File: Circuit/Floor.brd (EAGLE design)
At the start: 52.5 x 84.9 mm, 27 parts, among them U1 AMS1117-3.3, X2 ESP-12

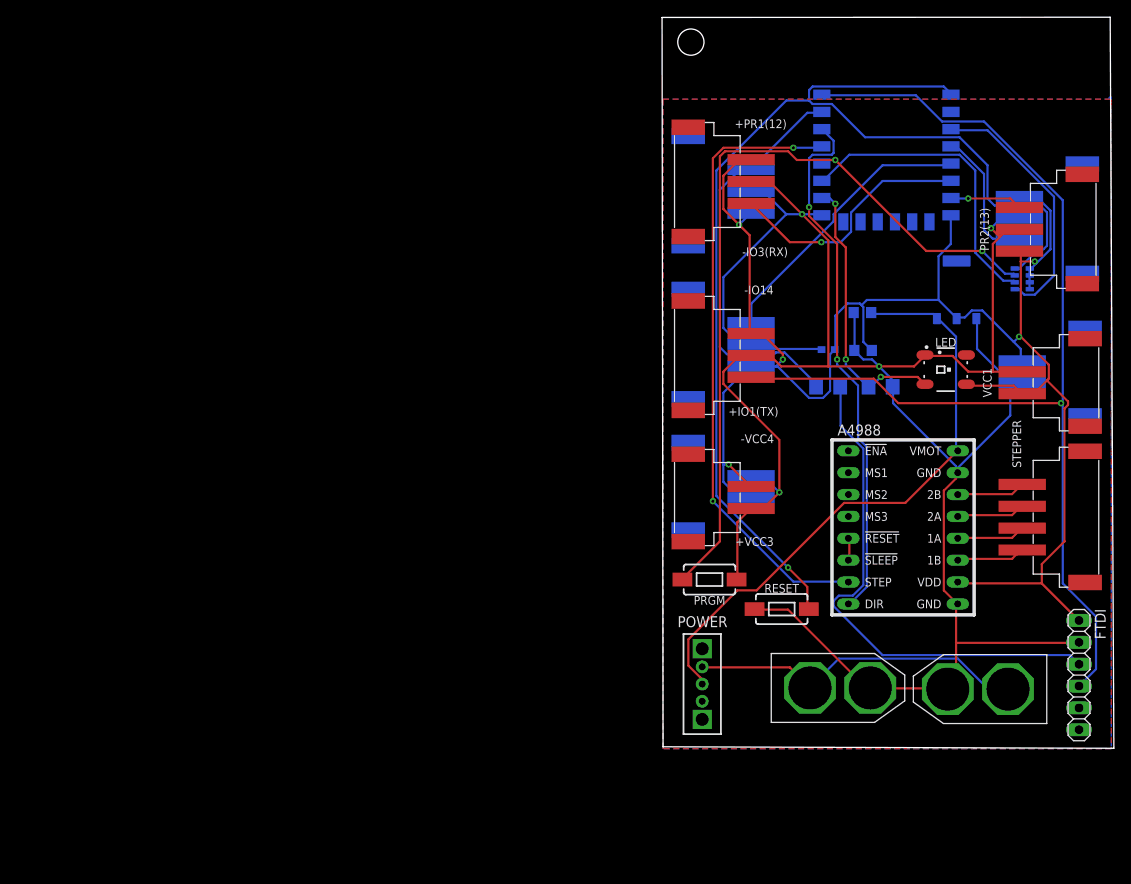
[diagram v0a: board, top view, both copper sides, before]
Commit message: correct flipped xh conns
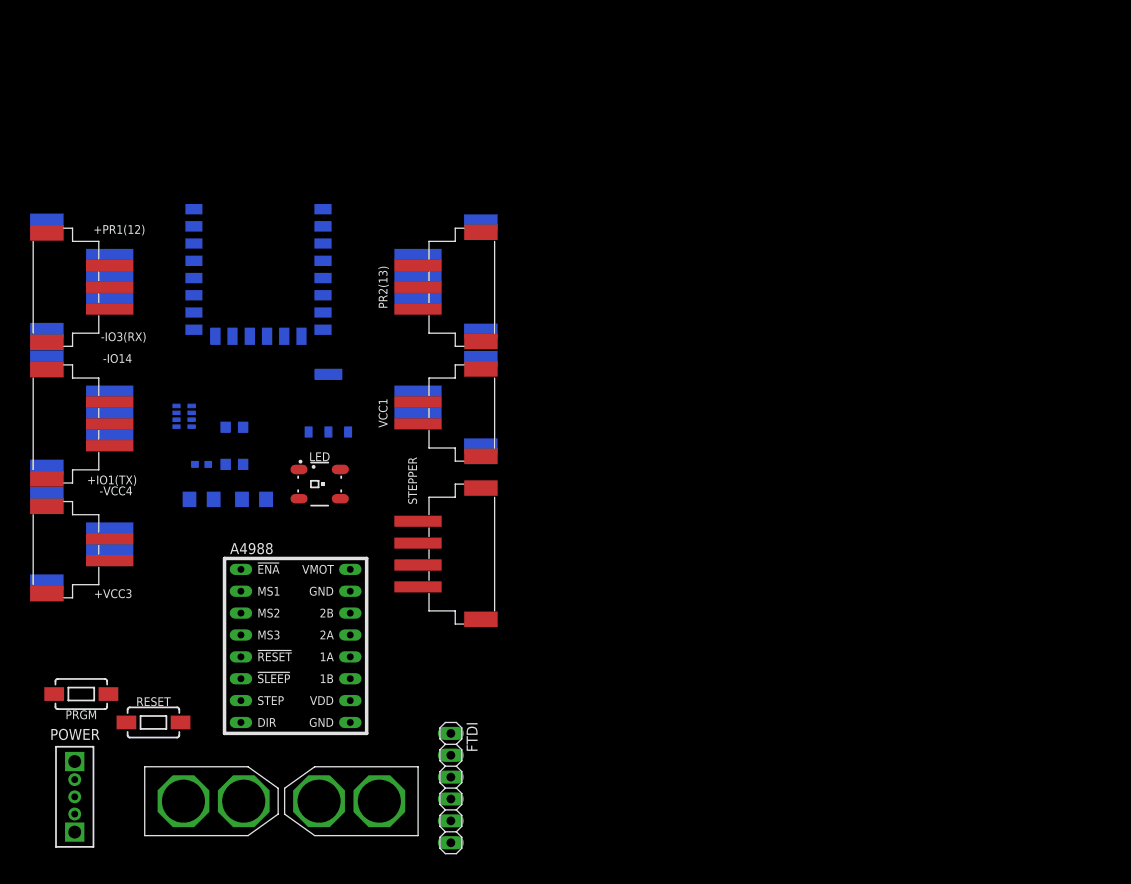
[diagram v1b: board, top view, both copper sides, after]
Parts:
- X2: device microbuilder:ESP-12E -> AutoPark:MICROBUILDER_ESP-12E
- moved RN1 98.7 mm to (18.0, 53.3)
- moved +PR1(12) 75.5 mm to (4.06, 68.3)
- moved -IO3(RX) 75.1 mm to (4.06, 69.6)
- moved +IO1(TX) 74.9 mm to (4.06, 52.5)
- moved -IO14 74.9 mm to (4.06, 53.7)
- moved +VCC3 74.7 mm to (4.06, 37.8)
- moved -VCC4 74.7 mm to (4.06, 39.1)
- moved C8 74.2 mm to (23.9, 47.8)
- moved U$9 74.2 mm to (45.2, 8.64)
- moved PRGM 74.2 mm to (6.10, 21.1)
- moved C6 74.1 mm to (23.9, 52.1)
- moved RESET 74.1 mm to (14.5, 17.8)
- moved U1 74.1 mm to (34.8, 54.9)
- moved X2 74.1 mm to (26.7, 71.6)
- moved FTDI 74.1 mm to (49.0, 10.2)
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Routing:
- net GND: track 276.7 -> 0.00 mm, vias 4 -> 0
- net 3.3V: track 205.0 -> 0.00 mm, vias 5 -> 0
- net RESET: track 131.8 -> 0.00 mm, vias 1 -> 0
- net TXD: track 129.4 -> 0.00 mm, vias 1 -> 0
- net GPIO0: track 93.2 -> 0.00 mm, vias 2 -> 0
- net GPIO4/SDA: track 72.7 -> 0.00 mm, vias 2 -> 0
- net VBAT: track 70.7 -> 0.00 mm
- net GPIO5/SCL: track 62.0 -> 0.00 mm, vias 2 -> 0
- net USB_RX: track 60.3 -> 0.00 mm
- net RXD: track 47.4 -> 0.00 mm
- net VIN: track 39.5 -> 0.00 mm
- net GPIO2: track 35.4 -> 0.00 mm
- net GPIO14/SCK: track 32.7 -> 0.00 mm
- net GPIO15: track 32.2 -> 0.00 mm, vias 3 -> 0
- net CH_PD: track 30.1 -> 0.00 mm
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- removed copper zone on layer 1, net GND
- removed copper zone on layer 16, net GND
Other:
- board outline removed

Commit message: floor pcb, led library, espnow wip
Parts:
- removed FTDI: (no value), pinhead:1X06
- added U$11: FTDI, AutoPark:1X06
- moved LED 30.4 mm to (9.91, 26.7)
- moved C7 7.62 mm to (27.7, 47.8), flipped to the top
- moved RN1 6.14 mm to (24.1, 54.1), flipped to the top
- moved C6 6.11 mm to (19.6, 47.8), flipped to the top
- moved RESET 2.59 mm to (15.0, 20.3)
- moved A4988 2.54 mm to (29.7, 27.9)
- moved PRGM 1.48 mm to (4.83, 20.3)
- moved U1 1.05 mm to (35.8, 54.6), flipped to the top
- flipped C8 to the top
- turned POWER to 0 degrees
- flipped R1 to the top
- flipped R2 to the top
- flipped X2 to the top
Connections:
- net 3.3V: now also U$11.VCC; no longer FTDI.1
- net GND: now also U$11.GND; no longer FTDI.2
- net TXD: now also U$11.RXD; no longer FTDI.4
- net USB_RX: now also U$11.TXD; no longer FTDI.3
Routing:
- net GND: track 0.00 -> 317.1 mm, vias 0 -> 3
- net 3.3V: track 0.00 -> 271.5 mm, vias 0 -> 4
- net TXD: track 0.00 -> 126.3 mm, vias 0 -> 2
- net GPIO0: track 0.00 -> 102.8 mm, vias 0 -> 2
- net GPIO5/SCL: track 0.00 -> 91.7 mm, vias 0 -> 1
- net GPIO4/SDA: track 0.00 -> 89.0 mm, vias 0 -> 1
- net VBAT: track 0.00 -> 87.1 mm
- net RXD: track 0.00 -> 78.5 mm, vias 0 -> 2
- net RESET: track 0.00 -> 69.7 mm, vias 0 -> 2
- net GPIO15: track 0.00 -> 62.4 mm
- net CH_PD: track 0.00 -> 54.0 mm
- net USB_RX: track 0.00 -> 51.8 mm, vias 0 -> 1
- net VIN: track 0.00 -> 39.4 mm
- net GPIO14/SCK: track 0.00 -> 38.1 mm, vias 0 -> 1
- net 1B: track 0.00 -> 35.6 mm
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- added copper zone on layer 1, net GND
- added copper zone on layer 16, net GND
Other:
- board outline added: 57.2 x 86.1 mm
- board text added: "AutoPark Floor"
- board text added: "V2 Feb 28, 2019"
